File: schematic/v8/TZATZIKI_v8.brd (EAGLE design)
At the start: 41.1 x 50.1 mm, 33 parts, among them J1 2X20-CHIP, P0 SE11, P1 SE11, P3 SE11, P4 SE11, U2 DS2431P

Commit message: added stereo poti pads
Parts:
- removed A_I, A_O: SE11, solpad:SE11
- removed SJ1: (no value), jumper:SJ
- added L_I, L_O, R_I, R_O: SE11, solpad:SE11
- added SJ3: (no value), jumper:SJ
- moved R1 6.12 mm to (41.8, 59.2)
- moved C5 5.51 mm to (38.3, 55.5)
- moved A_G 4.30 mm to (15.5, 63.0), turned to 180 degrees
- moved C4 3.20 mm to (34.6, 54.8)
- moved R2 2.90 mm to (34.6, 58.3)
- moved SJ2 1.93 mm to (34.5, 51.2), flipped to the bottom, turned to 90 degrees
- moved P3 1.26 mm to (31.0, 55.5)
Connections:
- removed net N$17: A_I.MP, J1.HPR, SJ1.2
- new net N$31: C4.2, R_I.MP, SJ2.2
- new net N$32: C5.2, L_I.MP, SJ3.2
- net N$15: now also L_O.MP, SJ3.1; no longer C5.2, SJ2.1
- net N$18: now also R_O.MP, SJ2.1; no longer C4.2, SJ2.2
- net N$30: now also J1.HPR; no longer A_O.MP, SJ1.1
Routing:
- net N$31: track 0.00 -> 23.3 mm
- net N$17: track 21.7 -> 0.00 mm, vias 1 -> 0
- net N$32: track 0.00 -> 21.0 mm, vias 0 -> 2
- net N$18: track 14.9 -> 34.8 mm, vias 2 -> 1
- net N$15: track 16.2 -> 35.7 mm, vias 2 -> 3
- net N$19: track 12.6 -> 6.21 mm
- net N$10: track 47.5 -> 51.8 mm
- net VOUT: track 29.1 -> 31.2 mm
- net N$7: track 57.6 -> 59.6 mm
- net N$22: track 2.50 -> 4.25 mm
- net N$24: track 20.0 -> 21.5 mm
- net N$30: track 15.4 -> 14.1 mm, vias 0 -> 1

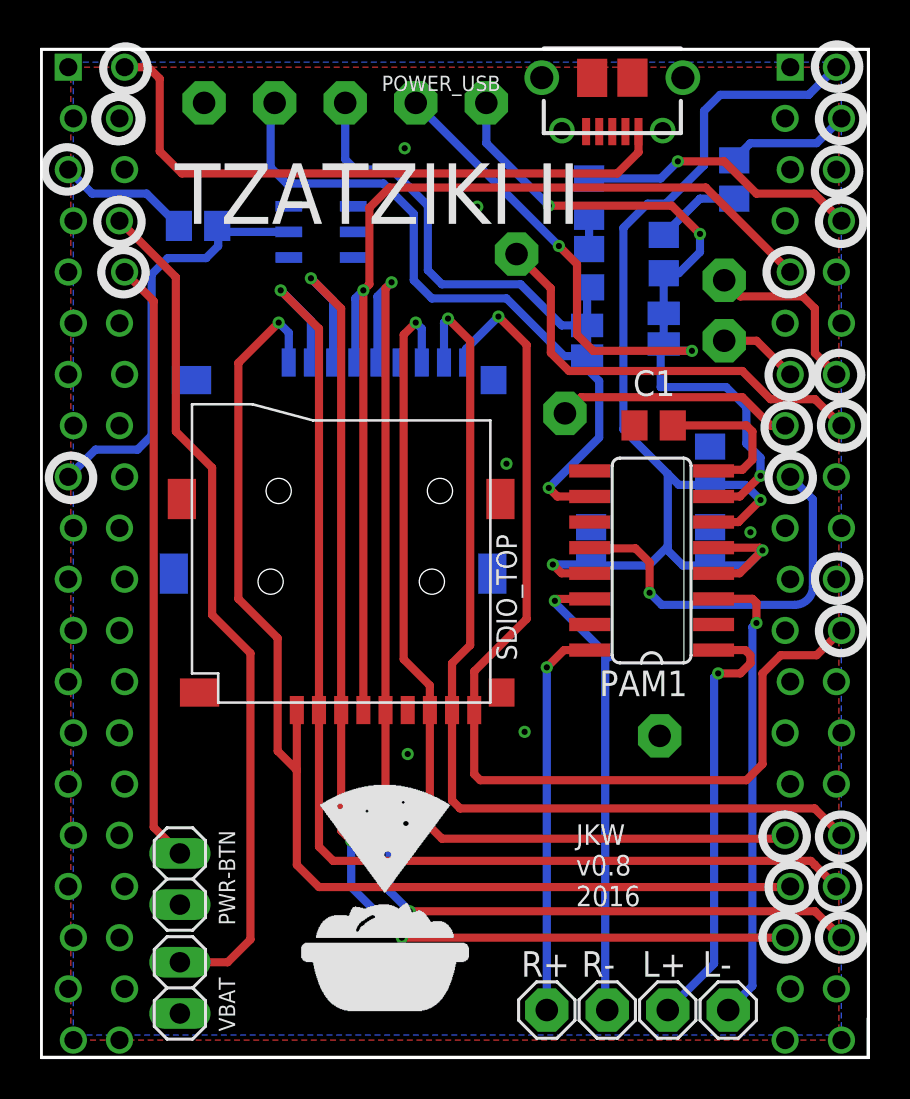
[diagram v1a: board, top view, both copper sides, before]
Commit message: added stereo pot, holes 0.9 todo
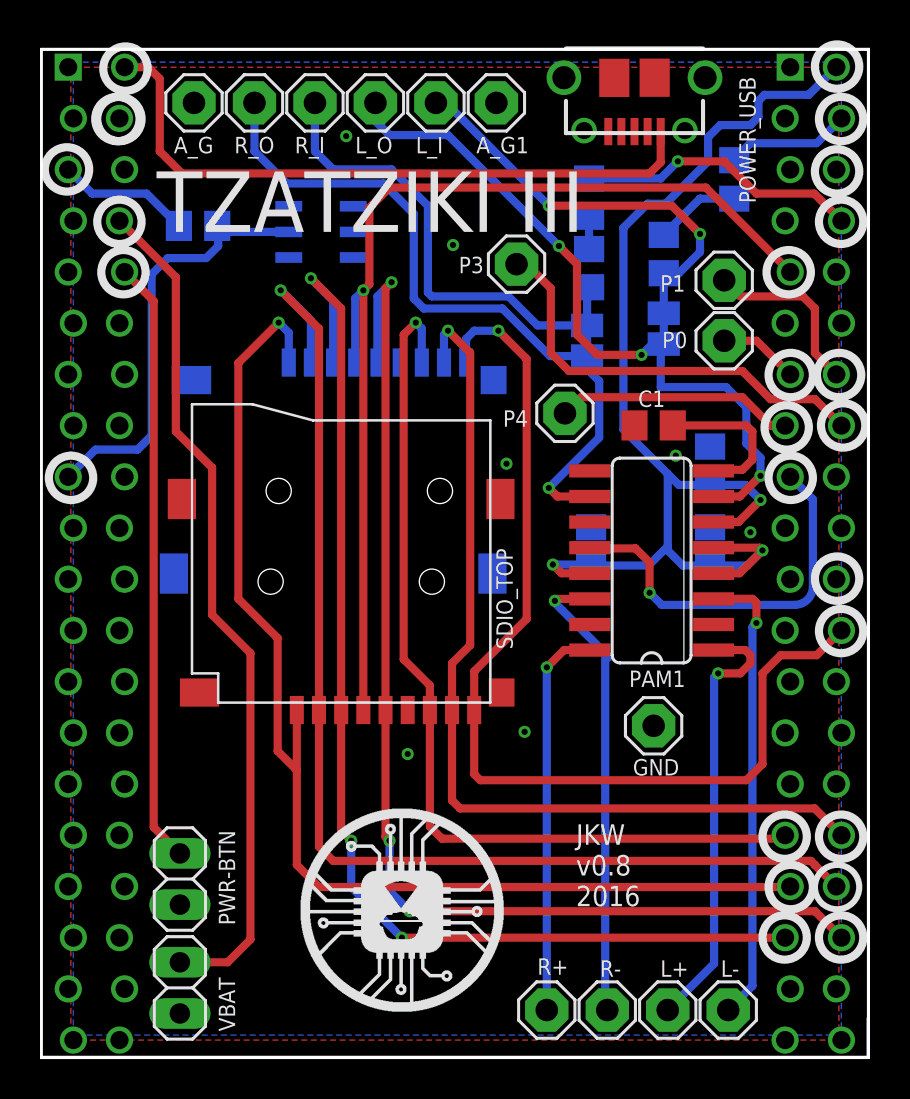
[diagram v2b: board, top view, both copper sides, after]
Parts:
- added A_G1: SE11, solpad:SE11
- U$1, U$2: device JKW_CHIP:LOGO_10X10_SILK -> JKW_CHIP:LOGO2_10X10_SILK
- moved U$2 2.78 mm to (29.2, 18.1)
- moved L_I 2.50 mm to (27.0, 63.0), flipped to the top
- moved L_O 2.00 mm to (24.0, 63.0), flipped to the top
- moved R_I 1.50 mm to (21.0, 63.0), flipped to the top
- moved POWER_USB 1.10 mm to (36.9, 64.2)
- moved R_O 1.00 mm to (18.0, 63.0), flipped to the top
- moved GND 0.58 mm to (37.8, 32.1), flipped to the top
- moved A_G 0.50 mm to (15.0, 63.0), flipped to the top
- moved P3 0.50 mm to (31.0, 55.0), flipped to the top
- flipped P0 to the top
- flipped P1 to the top
- flipped P4 to the top
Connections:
- net GND: now also A_G1.MP
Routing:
- net N$31: track 23.3 -> 25.2 mm
- net VOUT: track 31.2 -> 32.6 mm
- net N$32: track 21.0 -> 22.4 mm
- net N$6: track 47.0 -> 45.8 mm
- net N$18: track 34.8 -> 35.6 mm
- net N$16: track 51.4 -> 50.7 mm
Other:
- board text added: "TZATZIKI III"
- board text removed: "TZATZIKI II"
